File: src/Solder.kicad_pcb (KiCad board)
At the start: 2 copper layers, 135.9 x 275.4 mm, 9 parts, among them SW1 SW_Push

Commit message: Add decoration
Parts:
- removed the G*** at (94.2, 60.8)
- added G***: LOGO, LOGO, F.Cu at (118.5, 59.0)
- added G***: LOGO, LOGO, F.Cu at (150.0, 57.5)
- added RV1: R_Potentiometer, Potentiometer_THT:Potentiometer_Vishay_T73YP_Vertical, F.Cu at (99.0, 63.0)
- moved SW1 0.25 mm to (109.8, 57.2)
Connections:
- SW1 pad 2: Net-(D1-A) -> Net-(RV1-Pad2)
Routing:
- net Net-(BT1--): track 0.00 -> 30.4 mm
- net Net-(RV1-Pad2): track 0.00 -> 10.6 mm
- net Net-(D1-A): track 21.2 -> 22.6 mm
- net (no net): vias 1 -> 0
- removed copper zone on B.Cu, net Net-(BT1--)
- removed copper zone on F.Cu, net Net-(BT1--)

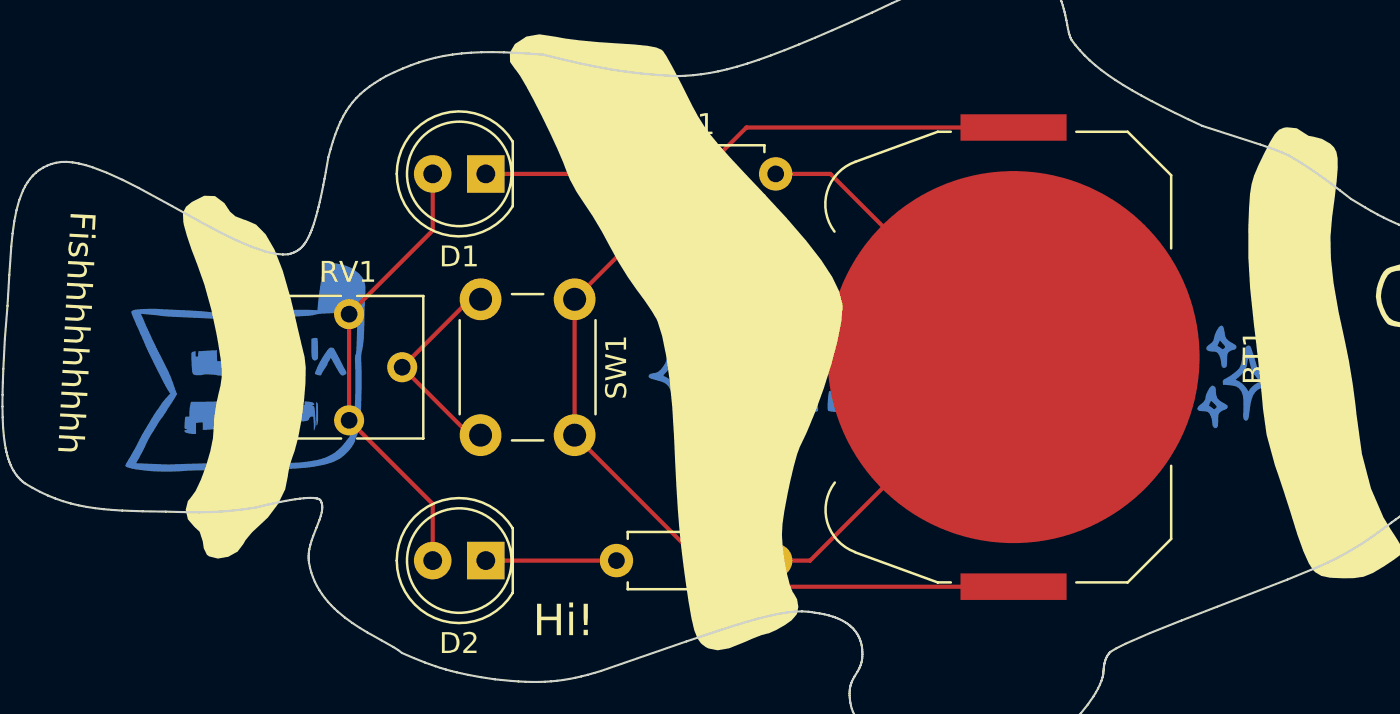
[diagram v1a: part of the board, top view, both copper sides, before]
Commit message: move back graphics to B.Silkscreen (not B.Cu)
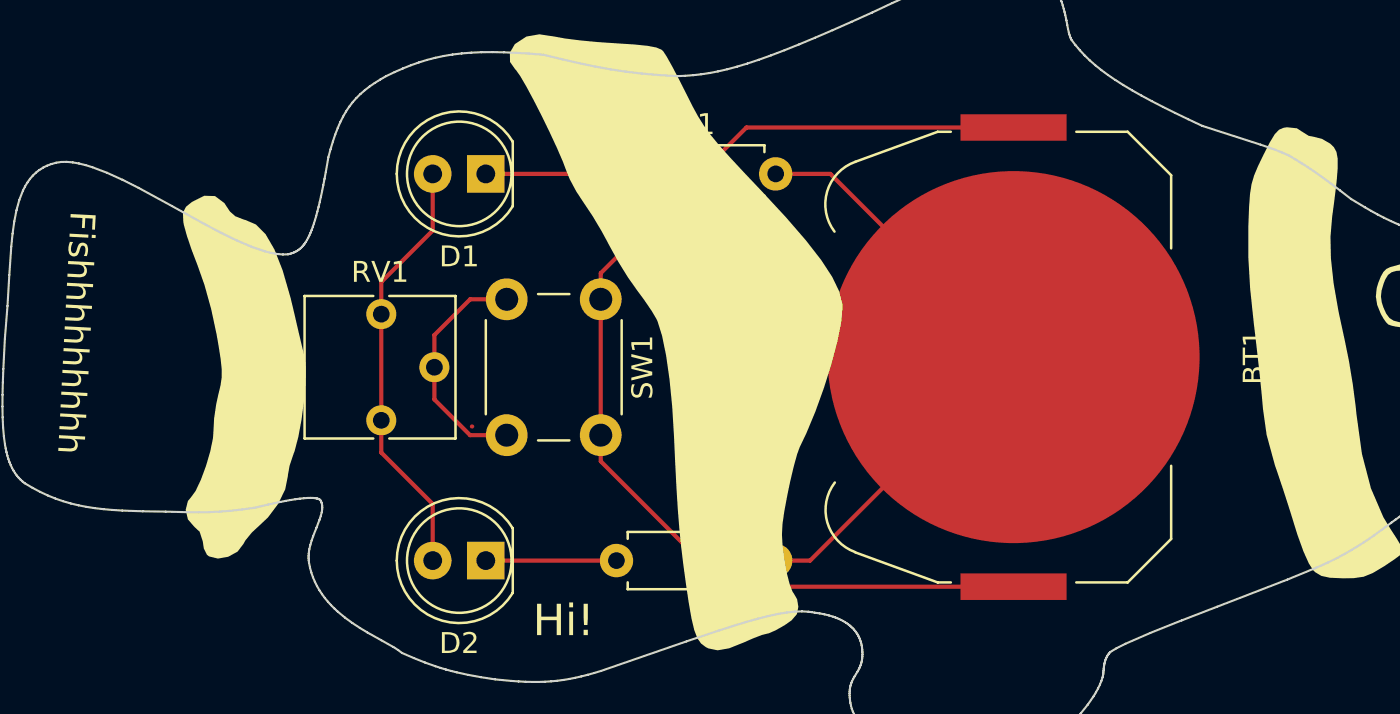
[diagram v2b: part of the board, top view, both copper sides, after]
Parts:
- removed the G*** at (128.2, 60.0)
- removed the G*** at (94.0, 60.5)
- added G***: LOGO, LOGO, B.Cu at (128.5, 60.0)
- added G***: LOGO, LOGO, B.Cu at (81.4, 69.8)
- moved RV1 1.54 mm to (100.5, 63.0)
- moved SW1 1.25 mm to (111.0, 57.2)
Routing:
- net Net-(D1-A): track 22.6 -> 21.3 mm
- net Net-(BT1-+): track 54.9 -> 53.9 mm
- net Net-(RV1-Pad2): track 10.6 -> 11.4 mm
